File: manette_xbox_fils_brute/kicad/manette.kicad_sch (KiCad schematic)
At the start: 33 parts, among them J1 THB001P, X1 SW_Push, Y1 SW_Push

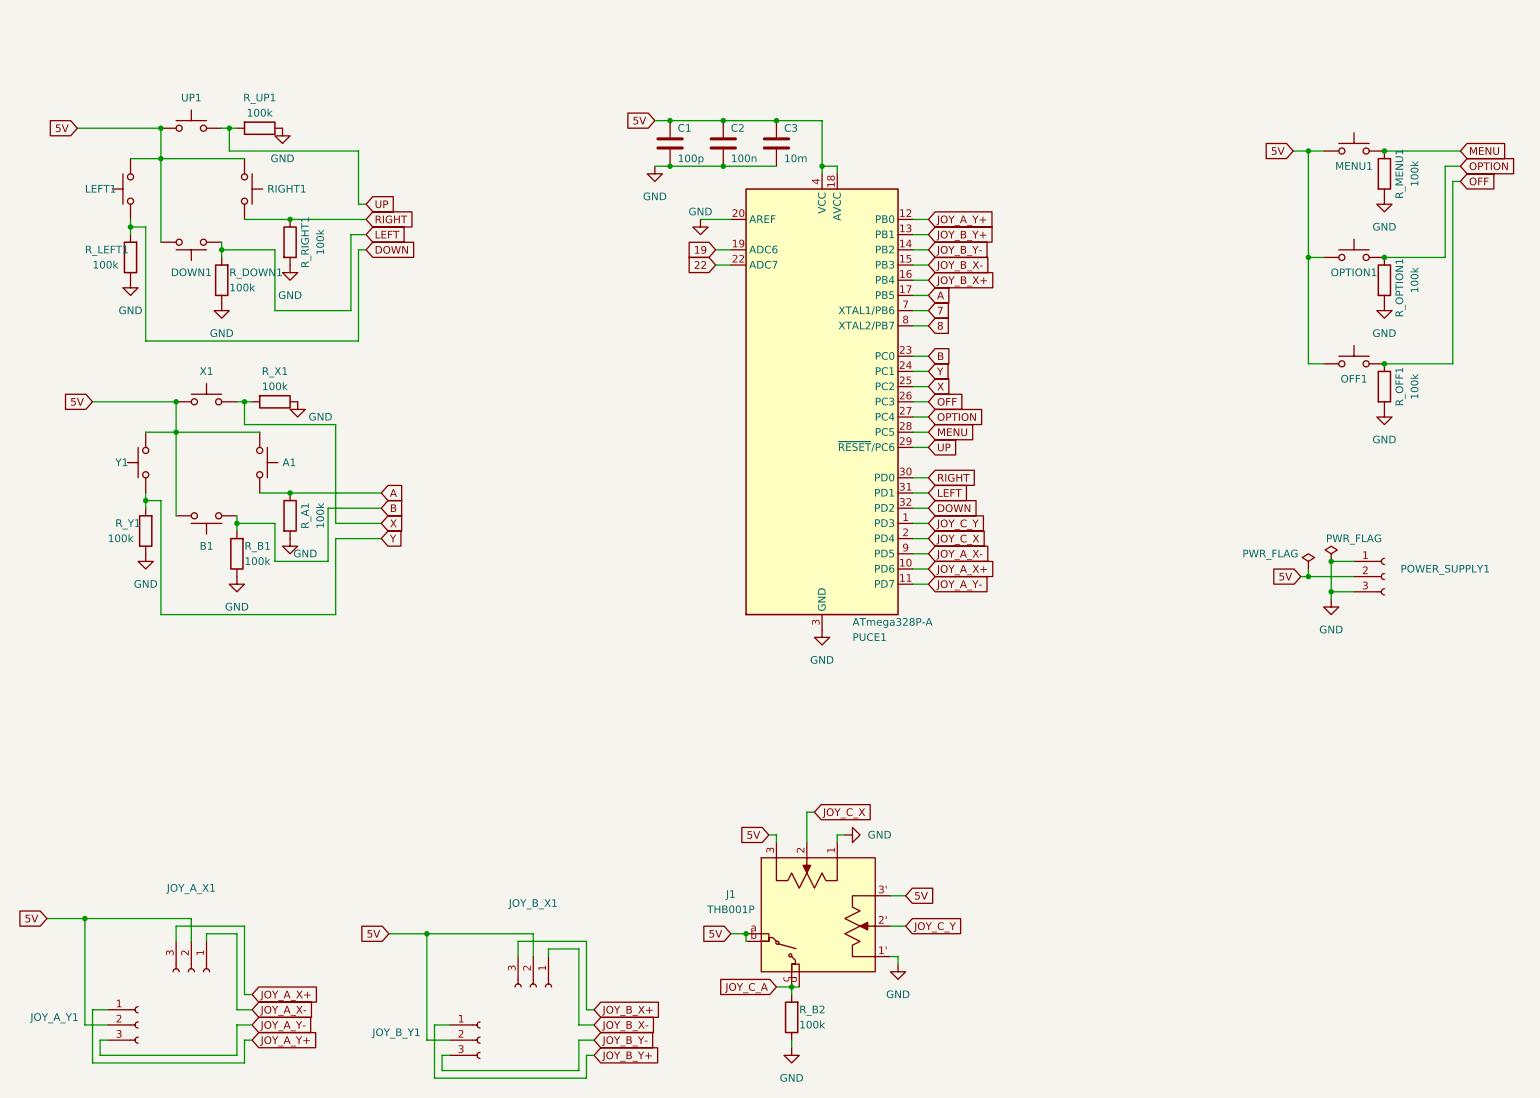
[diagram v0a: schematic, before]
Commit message: changement en version brut + ajout joystick générique
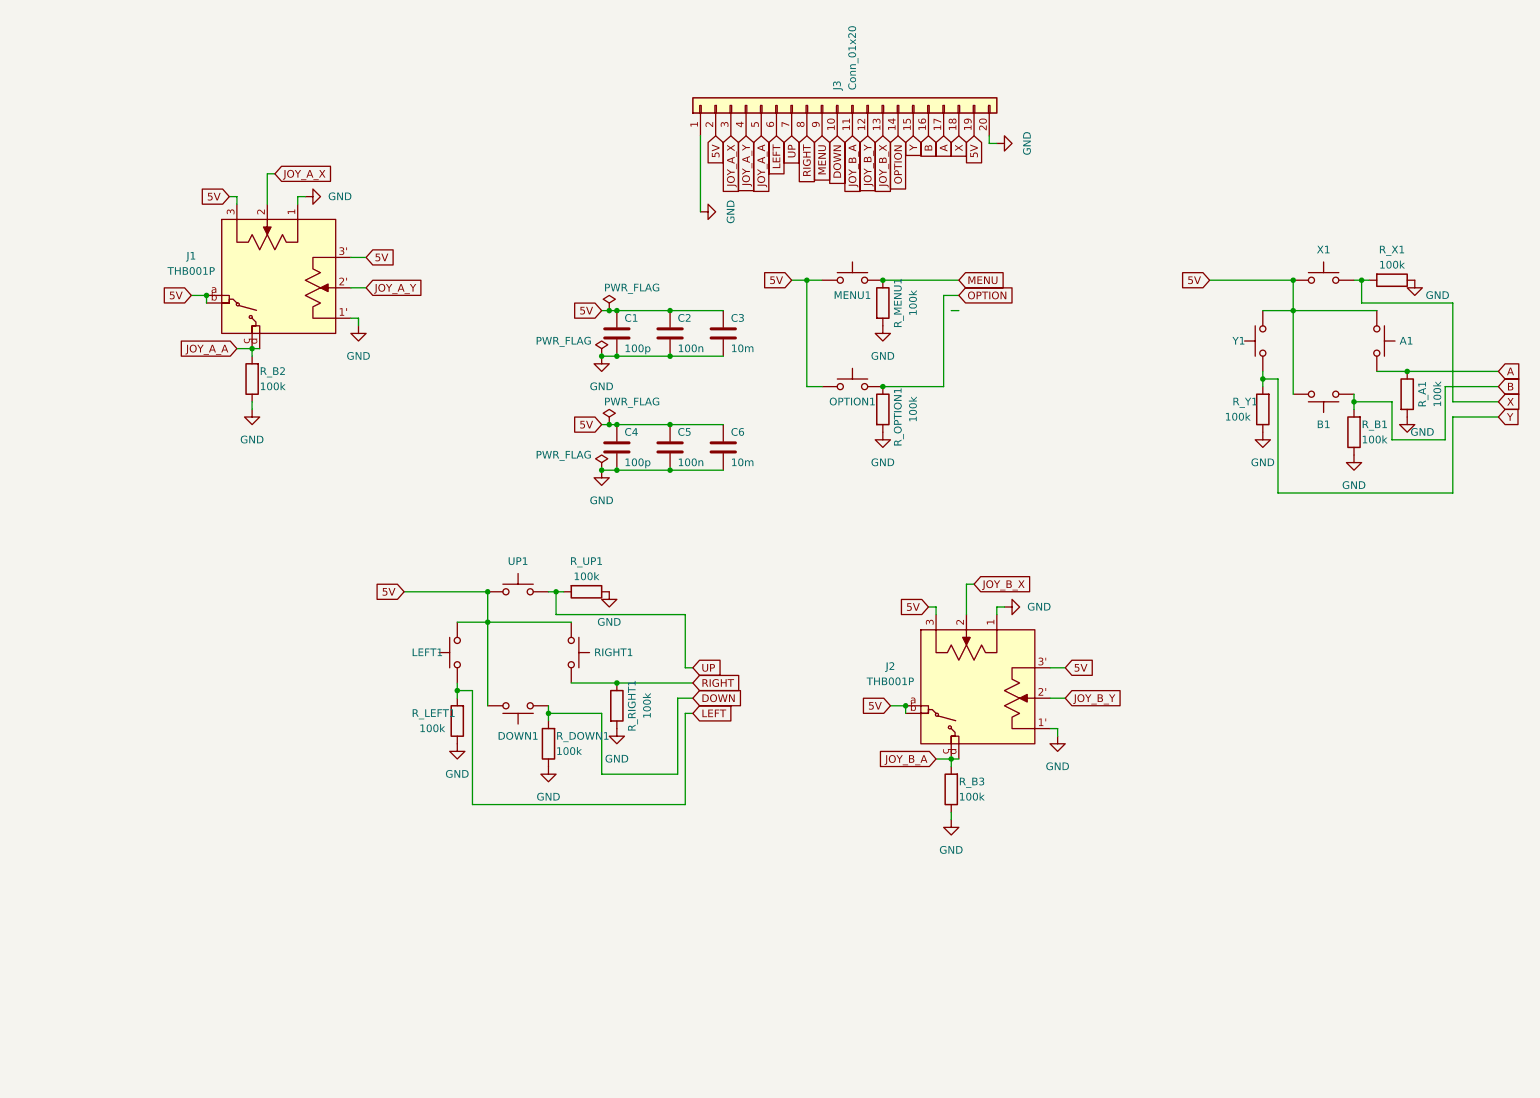
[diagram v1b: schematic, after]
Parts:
- removed JOY_A_X1, JOY_A_Y1, JOY_B_X1, JOY_B_Y1, POWER_SUPPLY1: Conn_01x03_Female, Connector_Wire:SolderWire-0.15sqmm_1x03_P4mm_D0.5mm_OD1.5mm, symbol Connector:Conn_01x03_Female
- removed OFF1: SW_Push, Button_Switch_THT:SW_PUSH_6mm_H9.5mm, symbol Switch:SW_Push
- removed PUCE1: ATmega328P-A, Package_QFP:TQFP-32_7x7mm_P0.8mm, symbol MCU_Microchip_ATmega:ATmega328P-A
- removed R_OFF1: 100k, Resistor_THT:R_Axial_DIN0411_L9.9mm_D3.6mm_P15.24mm_Horizontal, symbol Device:R
- added C4: 100p, Capacitor_THT:CP_Radial_D5.0mm_P2.50mm, symbol Device:C
- added C5: 100n, Capacitor_THT:CP_Radial_D5.0mm_P2.50mm, symbol Device:C
- added C6: 10m, Capacitor_THT:CP_Radial_D5.0mm_P2.50mm, symbol Device:C
- added J2: THB001P, LibPerso:Joystick_THB001P, symbol LibPerso:THB001P
- added J3: Conn_01x20, Connector_JST:JST_XH_B20B-XH-A_1x20_P2.50mm_Vertical, symbol Connector_Generic:Conn_01x20
- added R_B3: 100k, Resistor_THT:R_Axial_DIN0411_L9.9mm_D3.6mm_P15.24mm_Horizontal, symbol Device:R
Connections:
- net 5V: now also C4.1, C5.1, C6.1, J2.3, J2.3', J2.a, J2.b, J3.19 (Pin_19), J3.2 (Pin_2)
- net A: now also J3.17 (Pin_17)
- net B: now also J3.16 (Pin_16)
- net DOWN: now also DOWN1.1, R_DOWN1.2, J3.10 (Pin_10); no longer LEFT1.1, R_LEFT1.2
- net GND: now also C4.2, C5.2, C6.2, J2.1, J2.1', J3.1 (Pin_1), J3.20 (Pin_20), R_B3.1
- net LEFT: now also LEFT1.1, R_LEFT1.2, J3.6 (Pin_6); no longer DOWN1.1, R_DOWN1.2
- net MENU: now also J3.9 (Pin_9)
- net OPTION: now also J3.14 (Pin_14)
- net RIGHT: now also J3.8 (Pin_8)
- net UP: now also J3.7 (Pin_7)
- net X: now also J3.18 (Pin_18)
- net Y: now also J3.15 (Pin_15)
- net JOY_C_A renamed JOY_A_A
- net JOY_A_A: now also J3.5 (Pin_5)
- net JOY_C_X renamed JOY_A_X
- net JOY_A_X: now also J3.3 (Pin_3)
- net JOY_C_Y renamed JOY_A_Y
- net JOY_A_Y: now also J3.4 (Pin_4)
- new net JOY_B_A: J2.c, J2.d, J3.11 (Pin_11), R_B3.2
- new net JOY_B_X: J2.2, J3.13 (Pin_13)
- new net JOY_B_Y: J2.2', J3.12 (Pin_12)
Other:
- moved on the sheet: A1, B1, C1, C2, C3, DOWN1, J1, LEFT1, MENU1, OPTION1, RIGHT1, R_A1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
